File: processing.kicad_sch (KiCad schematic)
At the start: 62 parts, among them IC4 MT29F2G01ABAGDWB-IT_G_TR, IC5 MT29F2G01ABAGDWB-IT_G_TR, IC6 XMC7200D-E272K8384AA, IC7 DS90LV011AHMF_NOPB, Q1 ZXT849K, Y1 DSC1101DM2-012.0000, Y2 DSC1101DM2-125.0000T, Y3 DSC1101DM2-025.0000

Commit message: Some mild V3 changes
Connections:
- net CMOS_LVDS_CLK_IN: now also IC6.J3 (P24.0); no longer IC6.E1 (P7.0)
- net ECO_IN: now also IC6.M17 (P21.2); no longer IC6.M18 (P21.3)
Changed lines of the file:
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@@
 	(wire
 		(pts
-			(xy 158.75 168.91) (xy 191.77 168.91)
-		)
-		(stroke
-			(width 0)
-			(type default)
-		)
-	)
-	(wire
-		(pts
 			(xy 53.34 168.91) (xy 59.69 168.91)
 		)
@@
 	(wire
 		(pts
-			(xy 270.51 285.75) (xy 270.51 294.64)
+			(xy 267.97 285.75) (xy 267.97 294.64)
 		)
 		(stroke
@@
 	(wire
 		(pts
-			(xy 191.77 190.5) (xy 191.77 189.23)
+			(xy 105.41 66.04) (xy 105.41 67.31)
 		)
 		(stroke
@@
 	(wire
 		(pts
-			(xy 105.41 66.04) (xy 105.41 67.31)
+			(xy 90.17 64.77) (xy 90.17 66.04)
 		)
 		(stroke
@@
 	(wire
 		(pts
-			(xy 90.17 64.77) (xy 90.17 66.04)
+			(xy 175.26 24.13) (xy 175.26 35.56)
 		)
 		(stroke
@@
 	(wire
 		(pts
-			(xy 175.26 24.13) (xy 175.26 35.56)
+			(xy 41.91 34.29) (xy 31.75 34.29)
 		)
 		(stroke
@@
 	(wire
 		(pts
-			(xy 41.91 34.29) (xy 31.75 34.29)
+			(xy 69.85 66.04) (xy 80.01 66.04)
 		)
 		(stroke
@@
 	(wire
 		(pts
-			(xy 69.85 66.04) (xy 80.01 66.04)
+			(xy 170.18 265.43) (xy 191.77 265.43)
 		)
 		(stroke
@@
 	(wire
 		(pts
-			(xy 168.91 190.5) (xy 191.77 190.5)
-		)
-		(stroke
-			(width 0)
-			(type default)
-		)
-	)
-	(wire
-		(pts
 			(xy 125.73 67.31) (xy 125.73 69.85)
 		)
@@
 		)
 	)
-	(label "CMOS_LVDS_CLK_IN"
-		(at 158.75 168.91 0)
-		(effects
-			(font
-				(size 1.27 1.27)
-			)
-			(justify left bottom)
-		)
-	)
 	(label "QSPI_SCLK"
 		(at 180.975 267.97 0)
@@
 	)
 	(label "ECO_IN"
-		(at 270.51 294.64 90)
+		(at 267.97 294.64 90)
+		(effects
+			(font
+				(size 1.27 1.27)
+			)
+			(justify left bottom)
+		)
+	)
+	(label "CMOS_LVDS_CLK_IN"
+		(at 170.18 265.43 0)
 		(effects
 			(font
@@
 	(hierarchical_label "CMOS_MASTER_CLK (P7.2)"
 		(shape output)
-		(at 168.91 190.5 180)
+		(at 191.77 189.23 180)
 		(effects
 			(font

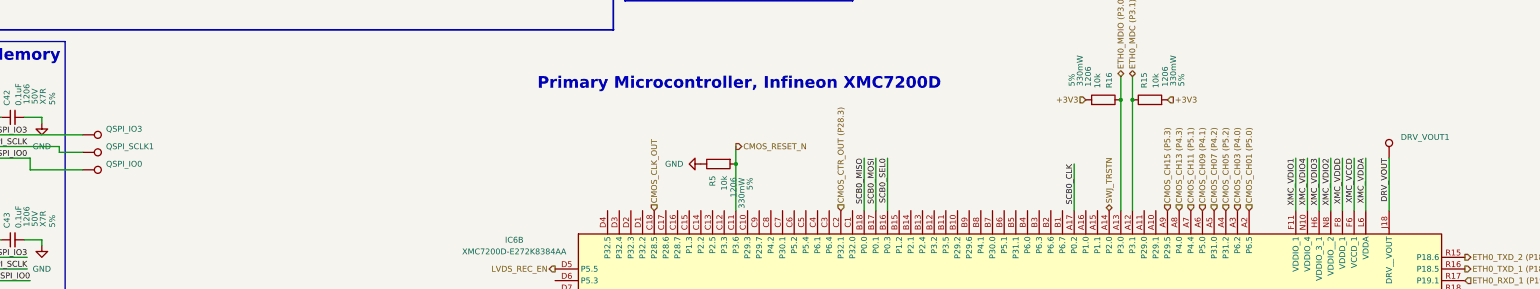
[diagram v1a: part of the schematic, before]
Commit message: V3 Almost Final
Move LVDS driver/change part if decided
Add thermal vias to GND pads of LDOs and ETH PHY.
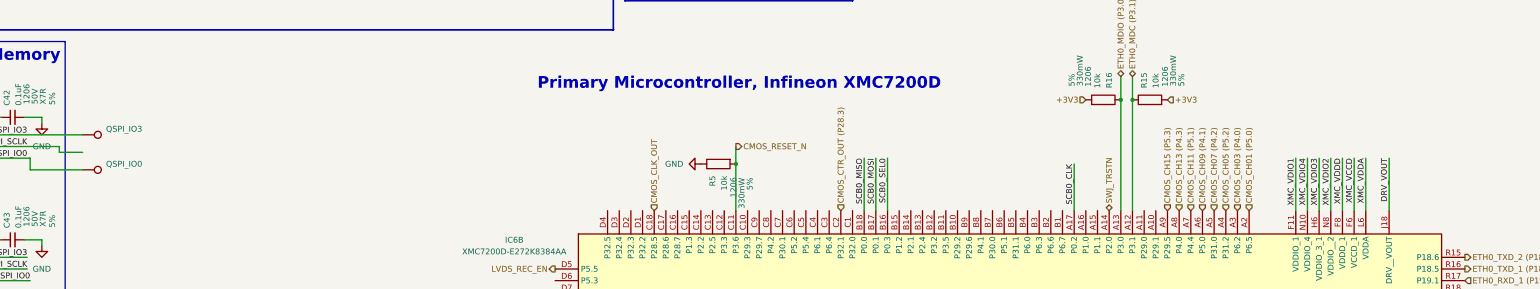
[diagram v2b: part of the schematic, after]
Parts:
- removed DRV_VOUT1: DRV_VOUT1, TestPoint:TestPoint_Pad_2.0x2.0mm, symbol Connector:TestPoint
- removed QSPI_SCLK1: QSPI_SCLK, TestPoint:TestPoint_Pad_2.0x2.0mm, symbol Connector:TestPoint
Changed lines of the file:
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@@
 	)
 	(symbol
-		(lib_id "Connector:TestPoint")
-		(at 88.9 110.49 270)
-		(unit 1)
-		(exclude_from_sim no)
-		(in_bom no)
-		(on_board yes)
-		(dnp no)
-		(property "Reference" "QSPI_SCLK1"
-			(at 93.98 109.2199 90)
-			(effects
-				(font
-					(size 1.27 1.27)
-				)
-				(justify left)
-			)
-		)
-		(property "Value" "QSPI_SCLK"
-			(at 93.98 111.7599 90)
-			(effects
-				(font
-					(size 1.27 1.27)
-				)
-				(justify left)
-				(hide yes)
-			)
-		)
-		(property "Footprint" "TestPoint:TestPoint_Pad_2.0x2.0mm"
-			(at 88.9 115.57 0)
-			(effects
-				(font
-					(size 1.27 1.27)
-				)
-				(hide yes)
-			)
-		)
-		(property "Datasheet" "~"
-			(at 88.9 115.57 0)
-			(effects
-				(font
-					(size 1.27 1.27)
-				)
-				(hide yes)
-			)
-		)
-		(property "Description" "test point"
-			(at 88.9 110.49 0)
-			(effects
-				(font
-					(size 1.27 1.27)
-				)
-				(hide yes)
-			)
-		)
-		(pin "1"
-		)
-		(instances
-			(project "S25-26"
-				(path "/6f4563ef-8a79-4567-b913-33c6dfb42b56/e295881b-793d-44b2-856b-25e9d19ba3af"
-					(reference "QSPI_SCLK1")
-					(unit 1)
-				)
-			)
-		)
-	)
-	(symbol
 		(lib_id "Device:C_Small")
 		(at 82.55 38.1 0)
@@
 					(unit 1)
 				)
-			)
-		)
-	)
-	(symbol
-		(lib_id "Connector:TestPoint")
-		(at 373.38 111.76 0)
-		(unit 1)
-		(exclude_from_sim no)
-		(in_bom no)
-		(on_board yes)
-		(dnp no)
-		(property "Reference" "DRV_VOUT1"
-			(at 375.92 107.1879 0)
-			(effects
-				(font
-					(size 1.27 1.27)
-				)
-				(justify left)
-			)
-		)
-		(property "Value" "DRV_VOUT1"
-			(at 375.92 109.7279 0)
-			(effects
-				(font
-					(size 1.27 1.27)
-				)
-				(justify left)
-				(hide yes)
-			)
-		)
-		(property "Footprint" "TestPoint:TestPoint_Pad_2.0x2.0mm"
-			(at 378.46 111.76 0)
-			(effects
-				(font
-					(size 1.27 1.27)
-				)
-				(hide yes)
-			)
-		)
-		(property "Datasheet" "~"
-			(at 378.46 111.76 0)
-			(effects
-				(font
-					(size 1.27 1.27)
-				)
-				(hide yes)
-			)
-		)
-		(property "Description" "test point"
-			(at 373.38 111.76 0)
-			(effects
-				(font
-					(size 1.27 1.27)
-				)
-				(hide yes)
-			)
-		)
-		(pin "1"
-		)
-		(instances
-			(project "S25-26"
-				(path "/6f4563ef-8a79-4567-b913-33c6dfb42b56/e295881b-793d-44b2-856b-25e9d19ba3af"
-					(reference "DRV_VOUT1")
-					(unit 1)
-				)

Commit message: Keepouts on mounting holes, QSPI on different lines, new LVDS clock buffer, voltage sense circuit
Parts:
- removed C63: 0.1uF, Capacitor_SMD:C_1206_3216Metric, symbol Device:C_Polarized
- removed C64: 0.01uF, Capacitor_SMD:C_1206_3216Metric, symbol Device:C_Small
- removed IC7: DS90LV011AHMF_NOPB, SamacSys_Parts:SOT95P280X145-5N, symbol SamacSys_Parts:DS90LV011AHMF_NOPB
- added C107: 0.1uF, Capacitor_SMD:C_0603_1608Metric, symbol Device:C_Small
- added R20: 50, Resistor_SMD:R_1206_3216Metric, symbol Device:R
- added R21: 22k, Resistor_SMD:R_1206_3216Metric, symbol Device:R
- added R27: 33k, Resistor_SMD:R_1206_3216Metric, symbol Device:R
- added R28, R29: 10k, Resistor_SMD:R_1206_3216Metric, symbol Device:R
- added RLVDS12, RLVDS13, RLVDS14: 100, Resistor_SMD:R_0603_1608Metric, symbol Device:R_Small
- added U5: LMK1D1204RGTT, SamacSys_Parts:VQFN16_RGT_TEX, symbol SamacSys_Parts:LMK1D1204RGTT
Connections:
- net +3V3: now also C107.1, R27.1, R28.1, U5.5 (VDD)
- net CMOS_CLK_IN_N: now also U5.10 (OUT0_N)
- net CMOS_CLK_IN_P: now also U5.9 (OUT0_P)
- net CMOS_LVDS_CLK_IN: now also R20.2
- net GND: now also C107.2, R21.2, R29.2, U5.1 (GND), U5.17 (EPAD), U5.2 (IN_SEL)
- net QSPI_IO0: no longer IC5.5 (SI/IO0)
- net QSPI_IO1: no longer IC5.2 (SO/IO1)
- net QSPI_IO2: no longer IC5.3 (WP#/IO2)
- net QSPI_IO3: no longer IC5.7 (HOLD#/IO3)
- net QSPI_IO4: now reaches IC6.L4 (P25.4)
- net QSPI_IO4: now also IC5.5 (SI/IO0)
- net QSPI_IO5: now reaches IC6.M2 (P25.5)
- net QSPI_IO5: now also IC5.2 (SO/IO1)
- net QSPI_IO6: now reaches IC6.M3 (P25.6)
- net QSPI_IO6: now also IC5.3 (WP#/IO2)
- net QSPI_IO7: now reaches IC6.M4 (P25.7)
- net QSPI_IO7: now also IC5.7 (HOLD#/IO3)
- net VCC_ADC (P13.3): now reaches IC6.V4 (P13.3)
- net VCC_ADC (P13.3): now also R28.2, R29.1
- net TEMPR_ADC0 (P6.0) renamed TEMPR_ADC0 (P12.6)
- net TEMPR_ADC1 (P6.1) renamed TEMPR_ADC1 (P13.0)
- new net: RLVDS12.1, U5.16 (OUT3_N)
- new net: RLVDS12.2, U5.15 (OUT3_P)
- new net: RLVDS13.1, U5.14 (OUT2_N)
- new net: RLVDS13.2, U5.13 (OUT2_P)
- new net: RLVDS14.2, U5.11 (OUT1_P)
- new net: RLVDS14.1, U5.12 (OUT1_N)
- new net: R20.1, U5.6 (IN0_P)
- new net: R21.1, R27.2, U5.7 (IN0_N)
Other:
- note added: "Voltage Sense"
